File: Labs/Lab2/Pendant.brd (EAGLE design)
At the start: 50.8 x 50.8 mm, 24 parts

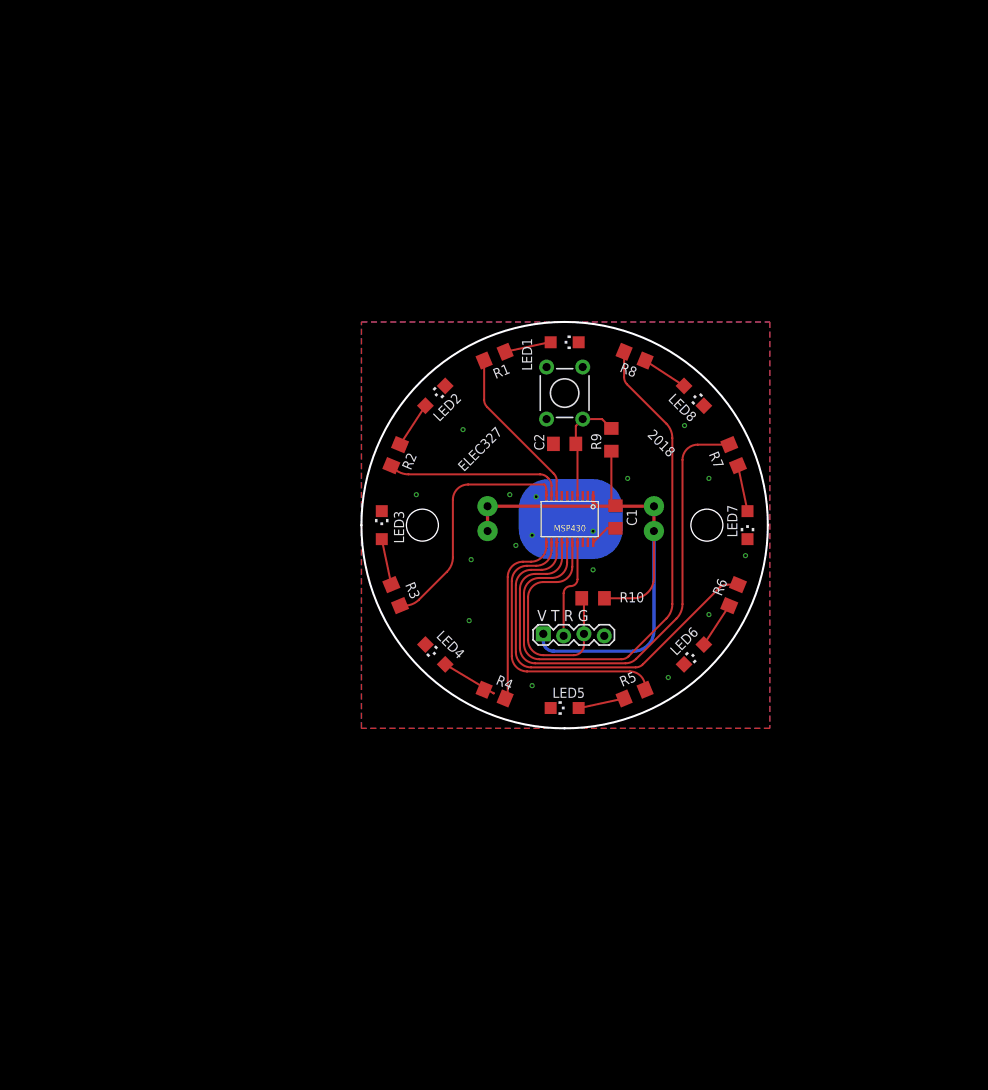
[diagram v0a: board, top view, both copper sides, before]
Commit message: Updated Pendant design for 2019
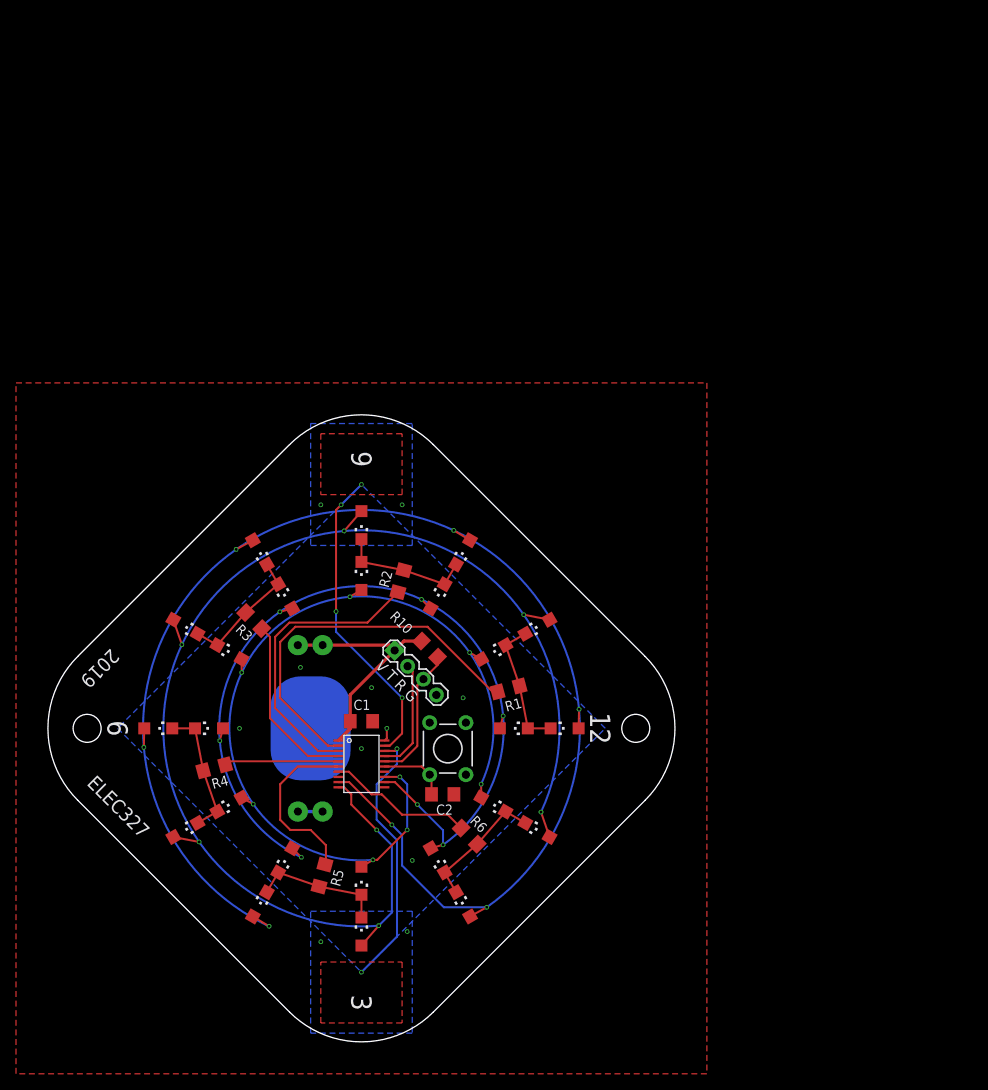
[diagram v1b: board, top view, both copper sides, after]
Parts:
- removed R7, R8, R9: (no value), rcl:R1206
- added LED10, LED11, LED12, LED13, LED14, LED15, LED16, LED17, LED18, LED19, LED20, LED21, LED22, LED23, LED24, LED9: (no value), led:CHIPLED_1206
- added LSP1, LSP10, LSP11, LSP12, LSP13, LSP14, LSP15, LSP16, LSP17, LSP18, LSP19, LSP2, LSP20, LSP21, LSP22, LSP23, LSP24, LSP3, LSP4, LSP5, LSP6, LSP7, LSP8, LSP9: LSP10, solpad-mod:LSP10
- moved LED1 48.3 mm to (25.4, 0.00), turned to 90 degrees
- moved S1 46.8 mm to (10.8, -2.54)
- moved C2 46.4 mm to (10.2, -8.26), turned to 180 degrees
- moved LED5 45.3 mm to (-12.7, -22.0), turned to 330 degrees
- moved R5 45.2 mm to (-4.93, -18.4), turned to 255 degrees
- moved R6 44.7 mm to (13.5, -13.5), turned to 315 degrees
- moved LED8 44.6 mm to (0.00, 25.4), turned to 180 degrees
- moved LED6 42.5 mm to (12.7, -22.0), turned to 30 degrees
- moved BAT1 41.7 mm to (-6.35, 0.00), turned to 270 degrees
- moved R1 41.6 mm to (18.4, 4.93), turned to 15 degrees
- moved C1 40.7 mm to (0.00, 0.89), turned to 0 degrees
- moved MSP430 40.2 mm to (0.00, -4.45), turned to 270 degrees
- moved R4 36.2 mm to (-18.4, -4.93), turned to 195 degrees
- moved LED4 35.8 mm to (-25.4, 0.00), turned to 270 degrees
- moved LED7 29.2 mm to (22.0, 12.7), turned to 120 degrees
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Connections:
- removed net D1: MSP430.8, R1.1
- removed net D2: MSP430.9, R2.1
- removed net D3: MSP430.10, R3.1
- removed net D4: MSP430.11, R4.1
- removed net D5: MSP430.12, R5.1
- removed net D6: MSP430.13, R6.1
- removed net D7: MSP430.14, R7.1
- removed net D8: MSP430.15, R8.1
- removed net N$14: C2.2, MSP430.4, R9.2, S1.3
- removed net N$2: LED2.A, R2.2
- new net CA1: LED1.C, LED13.C, LED19.C, LED7.C, R1.2
- new net CA2: LED14.C, LED2.C, LED20.C, LED8.C, R2.2
- new net CA3: LED15.C, LED21.C, LED3.C, LED9.C, R3.2
- new net CA4: LED10.C, LED16.C, LED22.C, LED4.C, R4.2
- new net CA5: LED11.C, LED17.C, LED23.C, LED5.C, R5.2
- new net CA6: LED12.C, LED18.C, LED24.C, LED6.C, R6.2
- new net CAP1: MSP430.19
- new net CAP2: MSP430.18
- new net CB1: LED1.A, LED2.A, LED3.A, LED4.A, LED5.A, LED6.A, LSP1.MP, LSP2.MP, LSP3.MP, LSP4.MP, LSP5.MP, LSP6.MP, MSP430.9
- new net CB2: LED10.A, LED11.A, LED12.A, LED7.A, LED8.A, LED9.A, LSP10.MP, LSP11.MP, LSP12.MP, LSP7.MP, LSP8.MP, LSP9.MP, MSP430.10
- new net CB3: LED13.A, LED14.A, LED15.A, LED16.A, LED17.A, LED18.A, LSP13.MP, LSP14.MP, LSP15.MP, LSP16.MP, LSP17.MP, LSP18.MP, MSP430.12
- new net CB4: LED19.A, LED20.A, LED21.A, LED22.A, LED23.A, LED24.A, LSP19.MP, LSP20.MP, LSP21.MP, LSP22.MP, LSP23.MP, LSP24.MP, MSP430.13
- new net N$9: MSP430.14
- new net SWITCH1: C2.2, MSP430.15, S1.1
- net GND: now also S1.3; no longer LED1.C, LED2.C, LED3.C, LED4.C, LED5.C, LED6.C, LED7.C, LED8.C, S1.1
- net N$1: now also MSP430.8; no longer LED1.A, R1.2
- net N$3: now also MSP430.2, R1.1; no longer LED3.A, R3.2
- net N$4: now also MSP430.3, R2.1; no longer LED4.A, R4.2
- net N$5: now also MSP430.4, R3.1; no longer LED5.A, R5.2
- net N$6: now also MSP430.5, R4.1; no longer LED6.A, R6.2
- net N$7: now also MSP430.6, R5.1; no longer LED7.A, R7.2
- net N$8: now also MSP430.7, R6.1; no longer LED8.A, R8.2
- net VDD: no longer R9.1
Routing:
- net CB1: track 0.00 -> 178.1 mm, vias 0 -> 1
- net CB2: track 0.00 -> 164.7 mm, vias 0 -> 1
- net CB3: track 0.00 -> 110.1 mm, vias 0 -> 1
- net CB4: track 0.00 -> 107.3 mm, vias 0 -> 2
- net D8: track 72.6 -> 0.00 mm
- net D7: track 66.0 -> 0.00 mm
- net D6: track 49.7 -> 0.00 mm
- net VDD: track 79.8 -> 33.5 mm
- net N$3: track 6.22 -> 48.1 mm
- net CAP1: track 0.00 -> 38.7 mm, vias 0 -> 4
- net D5: track 36.0 -> 0.00 mm
- net CAP2: track 0.00 -> 33.5 mm, vias 0 -> 2
- net D3: track 30.6 -> 0.00 mm
- net N$4: track 7.47 -> 36.7 mm
- net D4: track 22.9 -> 0.00 mm
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- added copper zone on layer 1, net CAP1
- added copper zone on layer 1, net CAP2
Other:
- board size 50.8 x 50.8 mm -> 78.4 x 78.4 mm
- board text added: "12"
- board text added: "2019"
- board text added: "3"
- board text added: "6"
- board text added: "9"
- board text added: "sdg"
- board text removed: "2018"
- board text removed: "MSP430"

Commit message: Updated pendant for 2021 (tic tac toe)
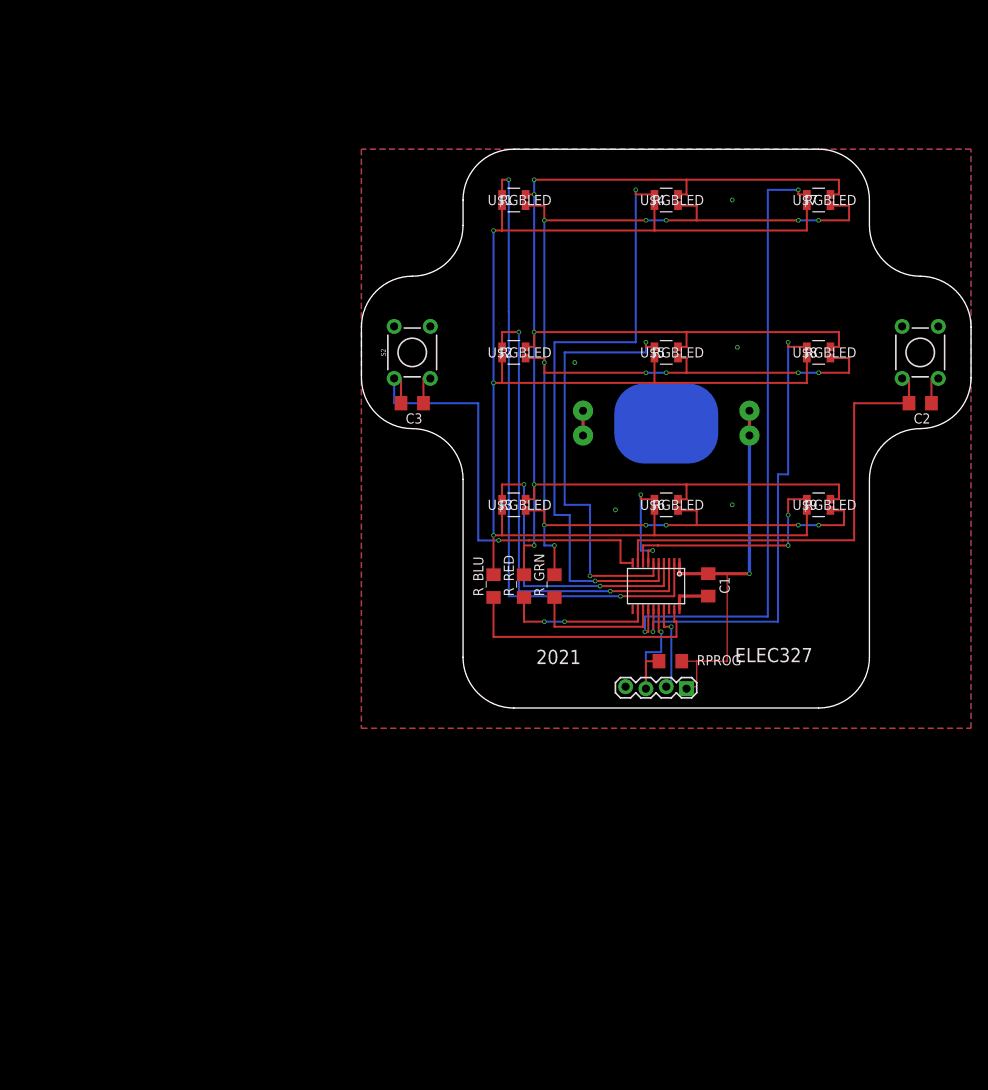
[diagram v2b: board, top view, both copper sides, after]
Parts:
- removed LED1, LED10, LED11, LED12, LED13, LED14, LED15, LED16, LED17, LED18, LED19, LED2, LED20, LED21, LED22, LED23, LED24, LED3, LED4, LED5, LED6, LED7, LED8, LED9: (no value), led:CHIPLED_1206
- removed LSP1, LSP10, LSP11, LSP12, LSP13, LSP14, LSP15, LSP16, LSP17, LSP18, LSP19, LSP2, LSP20, LSP21, LSP22, LSP23, LSP24, LSP3, LSP4, LSP5, LSP6, LSP7, LSP8, LSP9: LSP10, solpad-mod:LSP10
- removed R1, R10, R2, R3, R4, R5, R6: (no value), rcl:R1206
- added C3: 470nF, rcl:C1206
- added RPROG, R_BLU, R_GRN, R_RED: (no value), rcl:R1206
- added S2: MOMENTARY-SWITCH-SPST-PTH-6.0MM, SparkFun-Switches:TACTILE_SWITCH_PTH_6.0MM
- added U$1, U$2, U$3, U$4, U$5, U$6, U$7, U$8, U$9: RGBLED, RGB-LED:LED_TATRGB_INL
- moved C2 77.2 mm to (69.8, 40.6)
- moved S1 77.1 mm to (69.8, 47.0)
- moved BAT1 58.5 mm to (38.1, 38.1), turned to 0 degrees
- moved C1 46.6 mm to (43.4, 17.9), turned to 270 degrees
- moved MSP430 43.0 mm to (36.8, 17.8), turned to 180 degrees
- moved JP1 36.9 mm to (40.6, 5.08), turned to 180 degrees
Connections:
- removed net CAP1: MSP430.19
- removed net CAP2: MSP430.18
- removed net CB1: LED1.A, LED2.A, LED3.A, LED4.A, LED5.A, LED6.A, LSP1.MP, LSP2.MP, LSP3.MP, LSP4.MP, LSP5.MP, LSP6.MP, MSP430.9
- removed net CB2: LED10.A, LED11.A, LED12.A, LED7.A, LED8.A, LED9.A, LSP10.MP, LSP11.MP, LSP12.MP, LSP7.MP, LSP8.MP, LSP9.MP, MSP430.10
- removed net CB3: LED13.A, LED14.A, LED15.A, LED16.A, LED17.A, LED18.A, LSP13.MP, LSP14.MP, LSP15.MP, LSP16.MP, LSP17.MP, LSP18.MP, MSP430.12
- removed net CB4: LED19.A, LED20.A, LED21.A, LED22.A, LED23.A, LED24.A, LSP19.MP, LSP20.MP, LSP21.MP, LSP22.MP, LSP23.MP, LSP24.MP, MSP430.13
- removed net N$3: MSP430.2, R1.1
- removed net N$4: MSP430.3, R2.1
- removed net N$5: MSP430.4, R3.1
- removed net N$6: MSP430.5, R4.1
- removed net N$7: MSP430.6, R5.1
- removed net N$8: MSP430.7, R6.1
- removed net N$9: MSP430.14
- removed net SWITCH1: C2.2, MSP430.15, S1.1
- new net BLUE: R_BLU.2, U$1.3, U$2.3, U$3.3, U$4.3, U$5.3, U$6.3, U$7.3, U$8.3, U$9.3
- new net CA0: MSP430.2, U$1.1
- new net CA7: MSP430.15, U$8.1
- new net CA8: MSP430.8, U$9.1
- new net CB0: MSP430.19, R_BLU.1
- new net GREEN: R_GRN.2, U$1.4, U$2.4, U$3.4, U$4.4, U$5.4, U$6.4, U$7.4, U$8.4, U$9.4
- new net N$2: MSP430.13, R_GRN.1
- new net RED: R_RED.2, U$1.2, U$2.2, U$3.2, U$4.2, U$5.2, U$6.2, U$7.2, U$8.2, U$9.2
- new net SW0: C2.2, MSP430.9, S1.1
- new net SW1: C3.2, MSP430.10, S2.1
- net CA1: now also MSP430.3, U$2.1; no longer LED1.C, LED13.C, LED19.C, LED7.C, R1.2
- net CA2: now also MSP430.4, U$3.1; no longer LED14.C, LED2.C, LED20.C, LED8.C, R2.2
- net CA3: now also MSP430.5, U$4.1; no longer LED15.C, LED21.C, LED3.C, LED9.C, R3.2
- net CA4: now also MSP430.6, U$5.1; no longer LED10.C, LED16.C, LED22.C, LED4.C, R4.2
- net CA5: now also MSP430.7, U$6.1; no longer LED11.C, LED17.C, LED23.C, LED5.C, R5.2
- net CA6: now also MSP430.14, U$7.1; no longer LED12.C, LED18.C, LED24.C, LED6.C, R6.2
- net GND: now also C3.1, S2.3
- net N$1: now also MSP430.12, R_RED.1; no longer MSP430.8
- net VDD: now also RPROG.1; no longer R10.1
- net _RST: now also RPROG.2; no longer R10.2
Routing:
- net GREEN: track 0.00 -> 194.9 mm, vias 0 -> 16
- net RED: track 0.00 -> 189.3 mm, vias 0 -> 5
- net BLUE: track 0.00 -> 188.5 mm, vias 0 -> 3
- net CB1: track 178.1 -> 0.00 mm, vias 1 -> 0
- net CB2: track 164.7 -> 0.00 mm, vias 1 -> 0
- net CB3: track 110.1 -> 0.00 mm, vias 1 -> 0
- net CB4: track 107.3 -> 0.00 mm, vias 2 -> 0
- net CA0: track 0.00 -> 79.6 mm, vias 0 -> 2
- net CA6: track 16.5 -> 79.3 mm, vias 0 -> 2
- net CA3: track 16.5 -> 77.3 mm, vias 0 -> 2
- net CA7: track 0.00 -> 58.9 mm, vias 0 -> 2
- net SW0: track 0.00 -> 57.8 mm
- net SW1: track 0.00 -> 56.9 mm, vias 0 -> 1
- net N$3: track 48.1 -> 0.00 mm
- net CA1: track 16.5 -> 58.6 mm, vias 0 -> 2
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- removed copper zone on layer 1, net CAP1
- removed copper zone on layer 1, net CAP2
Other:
- board size 78.4 x 78.4 mm -> 76.2 x 69.8 mm
- board text added: "2021"
- board text removed: "12"
- board text removed: "2019"
- board text removed: "3"
- board text removed: "6"
- board text removed: "9"
- board text removed: "V T R G"

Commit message: Restored original 2020 pendant in directory, made a new directory for 2021 fabbed pendant, and a directory for Bonus PCB.
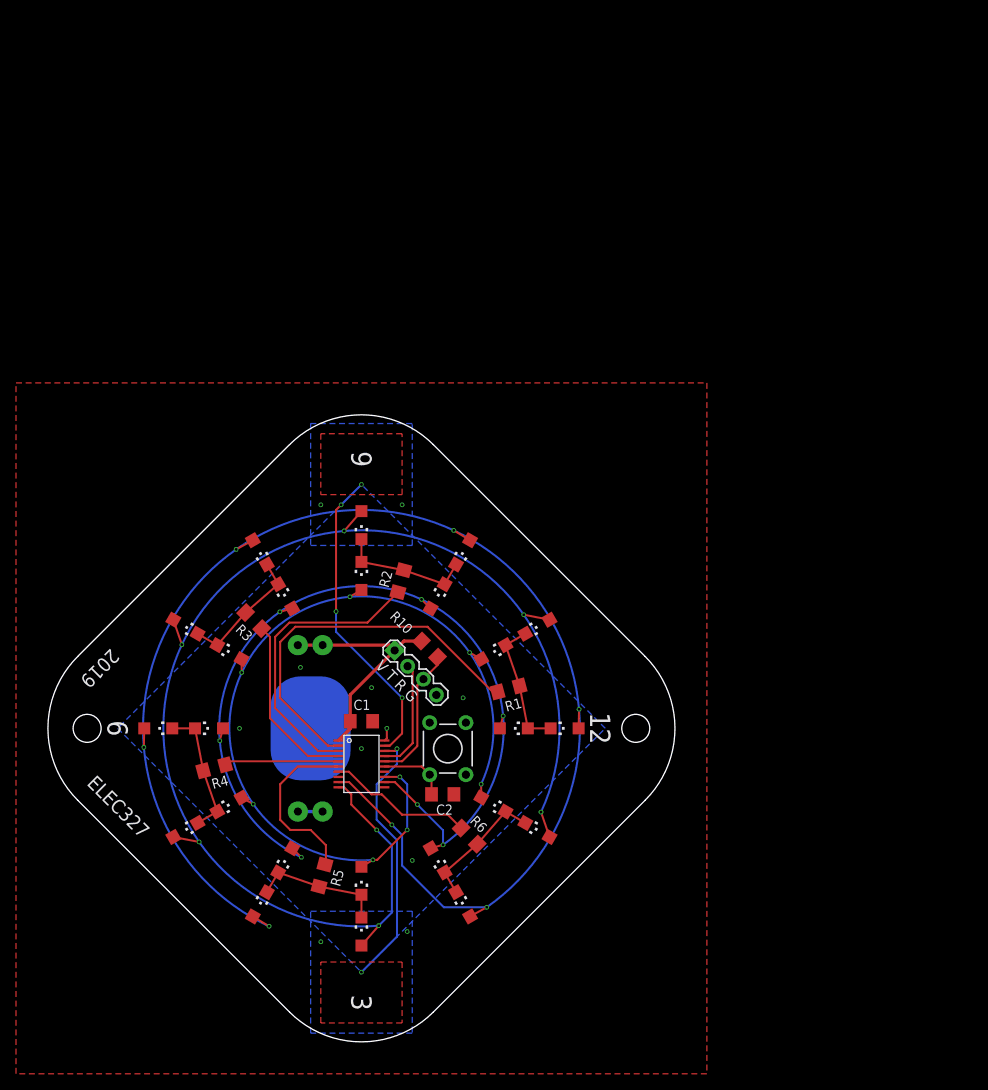
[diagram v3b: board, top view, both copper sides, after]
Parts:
- removed C3: 470nF, rcl:C1206
- removed RPROG, R_BLU, R_GRN, R_RED: (no value), rcl:R1206
- removed S2: MOMENTARY-SWITCH-SPST-PTH-6.0MM, SparkFun-Switches:TACTILE_SWITCH_PTH_6.0MM
- removed U$1, U$2, U$3, U$4, U$5, U$6, U$7, U$8, U$9: RGBLED, RGB-LED:LED_TATRGB_INL
- added LED1, LED10, LED11, LED12, LED13, LED14, LED15, LED16, LED17, LED18, LED19, LED2, LED20, LED21, LED22, LED23, LED24, LED3, LED4, LED5, LED6, LED7, LED8, LED9: (no value), led:CHIPLED_1206
- added LSP1, LSP10, LSP11, LSP12, LSP13, LSP14, LSP15, LSP16, LSP17, LSP18, LSP19, LSP2, LSP20, LSP21, LSP22, LSP23, LSP24, LSP3, LSP4, LSP5, LSP6, LSP7, LSP8, LSP9: LSP10, solpad-mod:LSP10
- added R1, R10, R2, R3, R4, R5, R6: (no value), rcl:R1206
- moved C2 77.2 mm to (10.2, -8.26)
- moved S1 77.1 mm to (10.8, -2.54)
- moved BAT1 58.5 mm to (-6.35, 0.00), turned to 270 degrees
- moved C1 46.6 mm to (0.00, 0.89), turned to 0 degrees
- moved MSP430 43.0 mm to (0.00, -4.45), turned to 270 degrees
- moved JP1 36.9 mm to (4.06, 9.65), turned to 315 degrees
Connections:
- removed net BLUE: R_BLU.2, U$1.3, U$2.3, U$3.3, U$4.3, U$5.3, U$6.3, U$7.3, U$8.3, U$9.3
- removed net CA0: MSP430.2, U$1.1
- removed net CA7: MSP430.15, U$8.1
- removed net CA8: MSP430.8, U$9.1
- removed net CB0: MSP430.19, R_BLU.1
- removed net GREEN: R_GRN.2, U$1.4, U$2.4, U$3.4, U$4.4, U$5.4, U$6.4, U$7.4, U$8.4, U$9.4
- removed net N$2: MSP430.13, R_GRN.1
- removed net RED: R_RED.2, U$1.2, U$2.2, U$3.2, U$4.2, U$5.2, U$6.2, U$7.2, U$8.2, U$9.2
- removed net SW0: C2.2, MSP430.9, S1.1
- removed net SW1: C3.2, MSP430.10, S2.1
- new net CAP1: MSP430.19
- new net CAP2: MSP430.18
- new net CB1: LED1.A, LED2.A, LED3.A, LED4.A, LED5.A, LED6.A, LSP1.MP, LSP2.MP, LSP3.MP, LSP4.MP, LSP5.MP, LSP6.MP, MSP430.9
- new net CB2: LED10.A, LED11.A, LED12.A, LED7.A, LED8.A, LED9.A, LSP10.MP, LSP11.MP, LSP12.MP, LSP7.MP, LSP8.MP, LSP9.MP, MSP430.10
- new net CB3: LED13.A, LED14.A, LED15.A, LED16.A, LED17.A, LED18.A, LSP13.MP, LSP14.MP, LSP15.MP, LSP16.MP, LSP17.MP, LSP18.MP, MSP430.12
- new net CB4: LED19.A, LED20.A, LED21.A, LED22.A, LED23.A, LED24.A, LSP19.MP, LSP20.MP, LSP21.MP, LSP22.MP, LSP23.MP, LSP24.MP, MSP430.13
- new net N$3: MSP430.2, R1.1
- new net N$4: MSP430.3, R2.1
- new net N$5: MSP430.4, R3.1
- new net N$6: MSP430.5, R4.1
- new net N$7: MSP430.6, R5.1
- new net N$8: MSP430.7, R6.1
- new net N$9: MSP430.14
- new net SWITCH1: C2.2, MSP430.15, S1.1
- net CA1: now also LED1.C, LED13.C, LED19.C, LED7.C, R1.2; no longer MSP430.3, U$2.1
- net CA2: now also LED14.C, LED2.C, LED20.C, LED8.C, R2.2; no longer MSP430.4, U$3.1
- net CA3: now also LED15.C, LED21.C, LED3.C, LED9.C, R3.2; no longer MSP430.5, U$4.1
- net CA4: now also LED10.C, LED16.C, LED22.C, LED4.C, R4.2; no longer MSP430.6, U$5.1
- net CA5: now also LED11.C, LED17.C, LED23.C, LED5.C, R5.2; no longer MSP430.7, U$6.1
- net CA6: now also LED12.C, LED18.C, LED24.C, LED6.C, R6.2; no longer MSP430.14, U$7.1
- net GND: no longer C3.1, S2.3
- net N$1: now also MSP430.8; no longer MSP430.12, R_RED.1
- net VDD: now also R10.1; no longer RPROG.1
- net _RST: now also R10.2; no longer RPROG.2
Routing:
- net GREEN: track 194.9 -> 0.00 mm, vias 16 -> 0
- net RED: track 189.3 -> 0.00 mm, vias 5 -> 0
- net BLUE: track 188.5 -> 0.00 mm, vias 3 -> 0
- net CB1: track 0.00 -> 178.1 mm, vias 0 -> 1
- net CB2: track 0.00 -> 164.7 mm, vias 0 -> 1
- net CB3: track 0.00 -> 110.1 mm, vias 0 -> 1
- net CB4: track 0.00 -> 107.3 mm, vias 0 -> 2
- net CA0: track 79.6 -> 0.00 mm, vias 2 -> 0
- net CA6: track 79.3 -> 16.5 mm, vias 2 -> 0
- net CA3: track 77.3 -> 16.5 mm, vias 2 -> 0
- net CA7: track 58.9 -> 0.00 mm, vias 2 -> 0
- net SW0: track 57.8 -> 0.00 mm
- net SW1: track 56.9 -> 0.00 mm, vias 1 -> 0
- net N$3: track 0.00 -> 48.1 mm
- net CA1: track 58.6 -> 16.5 mm, vias 2 -> 0
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- added copper zone on layer 1, net CAP1
- added copper zone on layer 1, net CAP2
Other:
- board size 76.2 x 69.8 mm -> 78.4 x 78.4 mm
- board text added: "12"
- board text added: "2019"
- board text added: "3"
- board text added: "6"
- board text added: "9"
- board text added: "V T R G"
- board text removed: "2021"
